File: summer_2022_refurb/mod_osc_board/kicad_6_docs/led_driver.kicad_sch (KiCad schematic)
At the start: 4 parts, among them U202 TL072

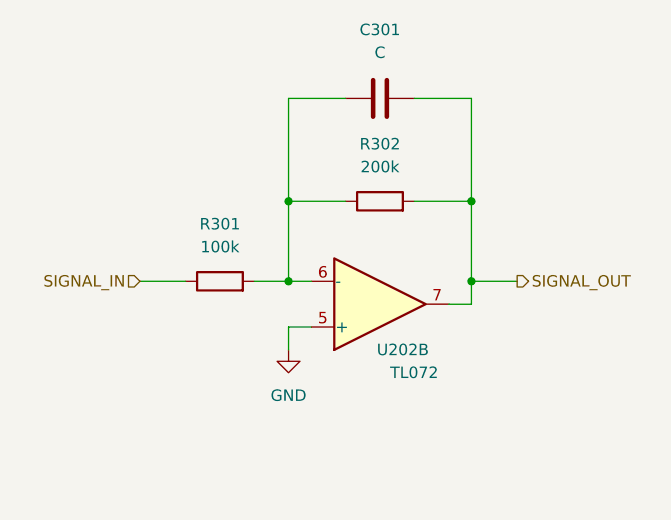
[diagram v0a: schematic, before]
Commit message: Change directory structure, minor schem and pcb tweaks
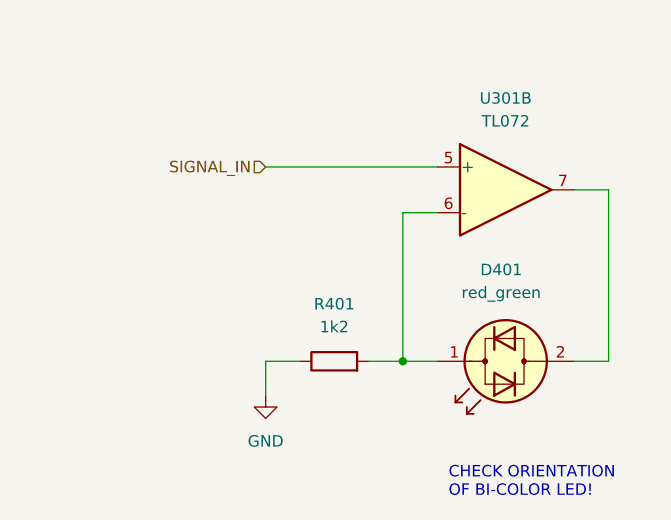
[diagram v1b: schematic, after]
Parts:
- removed C301: C, Capacitor_SMD:C_0805_2012Metric, symbol Device:C
- removed R301: 100k, Resistor_SMD:R_0805_2012Metric, symbol Device:R
- removed R302: 200k, Resistor_SMD:R_0805_2012Metric, symbol Device:R
- removed U202: TL072, Package_SO:SO-8_5.3x6.2mm_P1.27mm, symbol Amplifier_Operational:TL072
- added D401: red_green, LED_THT:LED_D5.0mm, symbol Device:LED_Dual_Bidirectional
- added R401: 1k2, Resistor_SMD:R_0805_2012Metric, symbol Device:R
- added U301: TL072, Package_SO:SO-8_5.3x6.2mm_P1.27mm, symbol Amplifier_Operational:TL072
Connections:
- net GND: now also R401.1
- net SIGNAL_IN: now also U301.5 (+)
- new net: D401.1 (KA), R401.2, U301.6 (-)
- new net: D401.2 (AK), U301.7
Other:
- note added: "CHECK ORIENTATION OF BI-COLOR LED!"
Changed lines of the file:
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@@
   (title_block
     (title "Josh Ox Ribbon Synth Mod Osc board")
-    (date "2022-06-12")
+    (date "2022-06-16")
     (rev "0")
     (comment 2 "creativecommons.org/licences/by/4.0")
@@
     (comment 4 "Author: Jordan Aceto")
   )
-  (junction (at 160.02 101.6) (diameter 0) (color 0 0 0 0)
+  (junction (at 152.4 110.49) (diameter 0) (color 0 0 0 0)
   )
-  (junction (at 139.7 101.6) (diameter 0) (color 0 0 0 0)
-  )
-  (junction (at 139.7 92.71) (diameter 0) (color 0 0 0 0)
-  )
-  (junction (at 160.02 92.71) (diameter 0) (color 0 0 0 0)
-  )
-  (wire (pts (xy 160.02 104.14) (xy 157.48 104.14))
+  (wire (pts (xy 137.16 114.3) (xy 137.16 110.49))
     (stroke (width 0) (type default) (color 0 0 0 0))
   )
-  (wire (pts (xy 139.7 109.22) (xy 139.7 106.68))
+  (wire (pts (xy 152.4 110.49) (xy 152.4 93.98))
     (stroke (width 0) (type default) (color 0 0 0 0))
   )
-  (wire (pts (xy 142.24 101.6) (xy 139.7 101.6))
+  (wire (pts (xy 137.16 110.49) (xy 140.97 110.49))
     (stroke (width 0) (type default) (color 0 0 0 0))
   )
-  (wire (pts (xy 153.67 92.71) (xy 160.02 92.71))
+  (wire (pts (xy 171.45 110.49) (xy 175.26 110.49))
     (stroke (width 0) (type default) (color 0 0 0 0))
   )
-  (wire (pts (xy 139.7 101.6) (xy 139.7 92.71))
+  (wire (pts (xy 148.59 110.49) (xy 152.4 110.49))
     (stroke (width 0) (type default) (color 0 0 0 0))
   )
-  (wire (pts (xy 139.7 81.28) (xy 139.7 92.71))
+  (wire (pts (xy 175.26 91.44) (xy 171.45 91.44))
     (stroke (width 0) (type default) (color 0 0 0 0))
   )
-  (wire (pts (xy 160.02 101.6) (xy 160.02 104.14))
+  (wire (pts (xy 156.21 110.49) (xy 152.4 110.49))
     (stroke (width 0) (type default) (color 0 0 0 0))
   )
-  (wire (pts (xy 135.89 101.6) (xy 139.7 101.6))
+  (wire (pts (xy 137.16 88.9) (xy 156.21 88.9))
     (stroke (width 0) (type default) (color 0 0 0 0))
   )
-  (wire (pts (xy 160.02 101.6) (xy 165.1 101.6))
+  (wire (pts (xy 175.26 110.49) (xy 175.26 91.44))
     (stroke (width 0) (type default) (color 0 0 0 0))
   )
-  (wire (pts (xy 153.67 81.28) (xy 160.02 81.28))
+  (wire (pts (xy 152.4 93.98) (xy 156.21 93.98))
     (stroke (width 0) (type default) (color 0 0 0 0))
   )
-  (wire (pts (xy 139.7 92.71) (xy 146.05 92.71))
-    (stroke (width 0) (type default) (color 0 0 0 0))
+  (text "CHECK ORIENTATION \nOF BI-COLOR LED!" (at 157.48 125.73 0)
+    (effects (font (size 1.27 1.27)) (justify left bottom))
   )
-  (wire (pts (xy 123.19 101.6) (xy 128.27 101.6))
-    (stroke (width 0) (type default) (color 0 0 0 0))
-  )
-  (wire (pts (xy 160.02 92.71) (xy 160.02 101.6))
-    (stroke (width 0) (type default) (color 0 0 0 0))
-  )
-  (wire (pts (xy 160.02 81.28) (xy 160.02 92.71))
-    (stroke (width 0) (type default) (color 0 0 0 0))
-  )
-  (wire (pts (xy 146.05 81.28) (xy 139.7 81.28))
-    (stroke (width 0) (type default) (color 0 0 0 0))
-  )
-  (wire (pts (xy 139.7 106.68) (xy 142.24 106.68))
-    (stroke (width 0) (type default) (color 0 0 0 0))
-  )
-  (hierarchical_label "SIGNAL_OUT" (shape output) (at 165.1 101.6 0)
-    (effects (font (size 1.27 1.27)) (justify left))
-  )
-  (hierarchical_label "SIGNAL_IN" (shape input) (at 123.19 101.6 180)
+  (hierarchical_label "SIGNAL_IN" (shape input) (at 137.16 88.9 180)
     (effects (font (size 1.27 1.27)) (justify right))
   )
-  (symbol (lib_id "power:GND") (at 139.7 109.22 0) (unit 1)
+  (symbol (lib_id "Amplifier_Operational:TL072") (at 163.83 91.44 0) (unit 2)
     (in_bom yes) (on_board yes) (fields_autoplaced)
-    (property "Reference" "#PWR0301" (id 0) (at 139.7 115.57 0)
+    (property "Reference" "U301" (id 0) (at 163.83 81.28 0))
+    (property "Value" "TL072" (id 1) (at 163.83 83.82 0))
+    (property "Footprint" "Package_SO:SO-8_5.3x6.2mm_P1.27mm" (id 2) (at 163.83 91.44 0)
       (effects (font (size 1.27 1.27)) hide)
     )
-    (property "Value" "GND" (id 1) (at 139.7 114.3 0))
-    (property "Footprint" "" (id 2) (at 139.7 109.22 0)
-      (effects (font (size 1.27 1.27)) hide)
-    )
-    (property "Datasheet" "" (id 3) (at 139.7 109.22 0)
-      (effects (font (size 1.27 1.27)) hide)
-    )
-    (pin "1")
-  )
-  (symbol (lib_id "Device:C") (at 149.86 81.28 90) (unit 1)
-    (in_bom yes) (on_board yes) (fields_autoplaced)
-    (property "Reference" "C301" (id 0) (at 149.86 73.66 90))
-    (property "Value" "C" (id 1) (at 149.86 76.2 90))
-    (property "Footprint" "Capacitor_SMD:C_0805_2012Metric" (id 2) (at 153.67 80.3148 0)
-      (effects (font (size 1.27 1.27)) hide)
-    )
-    (property "Datasheet" "~" (id 3) (at 149.86 81.28 0)
-      (effects (font (size 1.27 1.27)) hide)
-    )
-    (pin "1")
-    (pin "2")
-  )
-  (symbol (lib_id "Device:R") (at 132.08 101.6 90) (unit 1)
-    (in_bom yes) (on_board yes) (fields_autoplaced)
-    (property "Reference" "R301" (id 0) (at 132.08 95.25 90))
-    (property "Value" "100k" (id 1) (at 132.08 97.79 90))
-    (property "Footprint" "Resistor_SMD:R_0805_2012Metric" (id 2) (at 132.08 103.378 90)
-      (effects (font (size 1.27 1.27)) hide)
-    )
-    (property "Datasheet" "~" (id 3) (at 132.08 101.6 0)
-      (effects (font (size 1.27 1.27)) hide)
-    )
-    (pin "1")
-    (pin "2")
-  )
-  (symbol (lib_id "Amplifier_Operational:TL072") (at 149.86 104.14 0) (mirror x) (unit 2)
-    (in_bom yes) (on_board yes)
-    (property "Reference" "U202" (id 0) (at 152.4 109.22 0))
-    (property "Value" "TL072" (id 1) (at 153.67 111.76 0))
-    (property "Footprint" "Package_SO:SO-8_5.3x6.2mm_P1.27mm" (id 2) (at 149.86 104.14 0)
-      (effects (font (size 1.27 1.27)) hide)
-    )
-    (property "Datasheet" "http://www.ti.com/lit/ds/symlink/tl071.pdf" (id 3) (at 149.86 104.14 0)
+    (property "Datasheet" "http://www.ti.com/lit/ds/symlink/tl071.pdf" (id 3) (at 163.83 91.44 0)
       (effects (font (size 1.27 1.27)) hide)
     )
@@
     (pin "8")
   )
-  (symbol (lib_id "Device:R") (at 149.86 92.71 90) (unit 1)
+  (symbol (lib_id "power:GND") (at 137.16 114.3 0) (unit 1)
     (in_bom yes) (on_board yes) (fields_autoplaced)
-    (property "Reference" "R302" (id 0) (at 149.86 86.36 90))
-    (property "Value" "200k" (id 1) (at 149.86 88.9 90))
-    (property "Footprint" "Resistor_SMD:R_0805_2012Metric" (id 2) (at 149.86 94.488 90)
+    (property "Reference" "#PWR0401" (id 0) (at 137.16 120.65 0)
       (effects (font (size 1.27 1.27)) hide)
     )
-    (property "Datasheet" "~" (id 3) (at 149.86 92.71 0)
+    (property "Value" "GND" (id 1) (at 137.16 119.38 0))
+    (property "Footprint" "" (id 2) (at 137.16 114.3 0)
       (effects (font (size 1.27 1.27)) hide)
     )
+    (property "Datasheet" "" (id 3) (at 137.16 114.3 0)
+      (effects (font (size 1.27 1.27)) hide)
+    )
+    (pin "1")
+  )
+  (symbol (lib_id "Device:LED_Dual_Bidirectional") (at 163.83 110.49 180) (unit 1)
+    (in_bom yes) (on_board yes) (fields_autoplaced)
+    (property "Reference" "D401" (id 0) (at 163.3347 100.33 0))
+    (property "Value" "red_green" (id 1) (at 163.3347 102.87 0))
+    (property "Footprint" "LED_THT:LED_D5.0mm" (id 2) (at 163.83 110.49 0)
+      (effects (font (size 1.27 1.27)) hide)
+    )
+    (property "Datasheet" "~" (id 3) (at 163.83 110.49 0)
+      (effects (font (size 1.27 1.27)) hide)
+    )
+    (pin "1")
+    (pin "2")
+  )
+  (symbol (lib_id "Device:R") (at 144.78 110.49 90) (unit 1)
+    (in_bom yes) (on_board yes) (fields_autoplaced)
+    (property "Reference" "R401" (id 0) (at 144.78 104.14 90))
+    (property "Value" "1k2" (id 1) (at 144.78 106.68 90))
+    (property "Footprint" "Resistor_SMD:R_0805_2012Metric" (id 2) (at 144.78 112.268 90)
+      (effects (font (size 1.27 1.27)) hide)
+    )
+    (property "Datasheet" "~" (id 3) (at 144.78 110.49 0)
+      (effects (font (size 1.27 1.27)) hide)
+    )

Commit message: Buffer square, add saw polarity jumper
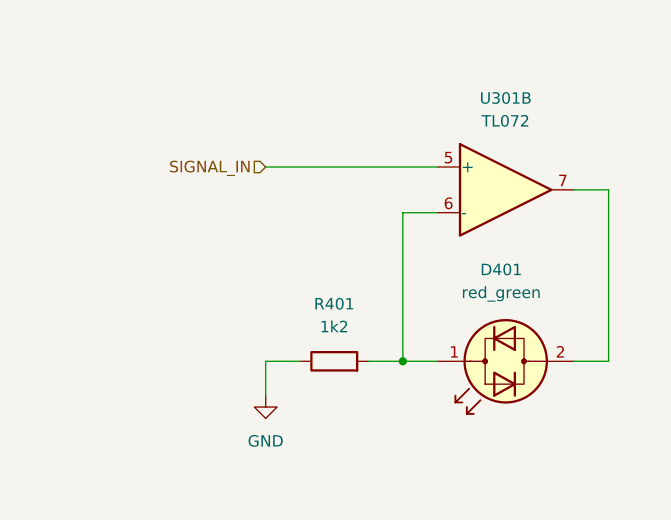
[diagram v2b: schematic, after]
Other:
- note removed: "CHECK ORIENTATION OF BI-COLOR LED!"
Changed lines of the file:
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@@
   (title_block
     (title "Josh Ox Ribbon Synth Mod Osc board")
-    (date "2022-06-16")
+    (date "2022-06-17")
     (rev "0")
     (comment 2 "creativecommons.org/licences/by/4.0")
@@
     (stroke (width 0) (type default) (color 0 0 0 0))
   )
-  (text "CHECK ORIENTATION \nOF BI-COLOR LED!" (at 157.48 125.73 0)
-    (effects (font (size 1.27 1.27)) (justify left bottom))
-  )
   (hierarchical_label "SIGNAL_IN" (shape input) (at 137.16 88.9 180)
